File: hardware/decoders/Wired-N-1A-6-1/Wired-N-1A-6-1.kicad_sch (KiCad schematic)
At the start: 53 parts, among them J0 CA, J1 CA, J10 RL, J11 RR, J12 FOF, J13 F0R, J14 MCLR, J15 +5, J16 GND, J17 PGD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

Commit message: Made Wired-N-1A-6-1 prettier, and easier to follow.
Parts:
- C11, C12: value 1uF -> 2.2uF; MPN1 (none) -> GRM155R6YA225KE11D; Specification 0805 50V 10uF X5R 10% -> 0402 35V 2.2uF X5R 10%
- C21, C23: MPN1 (none) -> GRM033R61E104KE14D; Specification 0402 50V 100nF X7R 10% -> 0201 25V 100nF X5R 10%
- C31: footprint Capacitor_SMD:C_0201_0603Metric -> Capacitor_SMD:C_0402_1005Metric; MPN1 (none) -> GRM155R61H104KE14D; Specification 0402 50V 100nF X7R 10% -> 0402 50V 100nF X5R 10%
- D11, D12, D13, D14: MPN1 (none) -> MSK4010
- J0, J1, J10, J11, J12, J13, J14, J15, J16, J17, J18, J2, J3, J4, J5, J6, J7, J8, J9: MPN1 (none) -> DNP; MPN2 (none) -> DNP
- Q31, Q32: MPN1 (none) -> QH8MA3 QH8MA3
- Q41, Q42, Q43, Q44: MPN1 (none) -> 2N7002KD
- R21, R36: MPN1 (none) -> 0201WMF1331TEE; MPN2 (none) -> RC0201FR-071K33L; Specification 0402 1.33K Ω 1% 1/8W -> 0201 1.33K Ω 1% 1/8W
- R22, R35: MPN1 (none) -> 0201WMF665KTEE; MPN2 (none) -> RC0603F6R65CS; Specification 0402 6.65K Ω 1% 1/8W -> 0201 6.65K Ω 1% 1/8W
- R23: MPN1 (none) -> 0201WMF1002TEE; MPN2 (none) -> RC0201FR-0710KL; Specification 0402 10K Ω 1% 1/8W -> 0201 10K Ω 1% 1/8W
- R31, R32, R33, R34, R41, R42, R43, R44, R45, R46, R47, R48: MPN1 (none) -> 0201WMF2200TEE; MPN2 (none) -> RC0201FR-07220RL; Specification 0402 220 Ω 1% 1/8W -> 0201 220 Ω 1% 1/8W
- U11: value LR8341A-T50 -> LR8341A; MPN1 (none) -> LR8341A-T50
- U21: value PIC18F06Q40 -> PIC18F; MPN1 (none) -> PIC18F06Q40
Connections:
- net BackEMF: now also U21.4 (PGM/C12IN3-/RC3); no longer U21.6 (RC7)
- net F0R: now also U21.6 (RC7); no longer U21.5 (T1CKI/SS1/RC6)
- net F6: now also U21.5 (T1CKI/SS1/RC6); no longer U21.4 (PGM/C12IN3-/RC3)

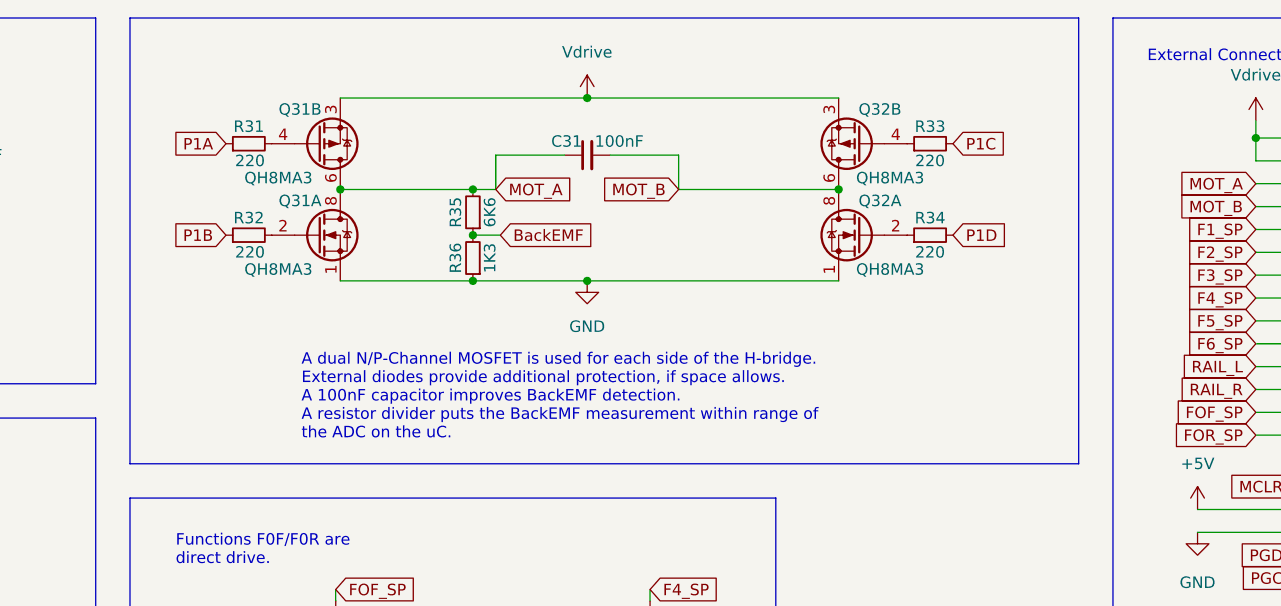
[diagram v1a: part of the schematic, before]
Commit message: Bring inline with Breadboard-1 reference design.
Add digital transitor drivers for the high side of the H-Bridge.
Add third BEMF resistor.
Relocate noise capacitor.
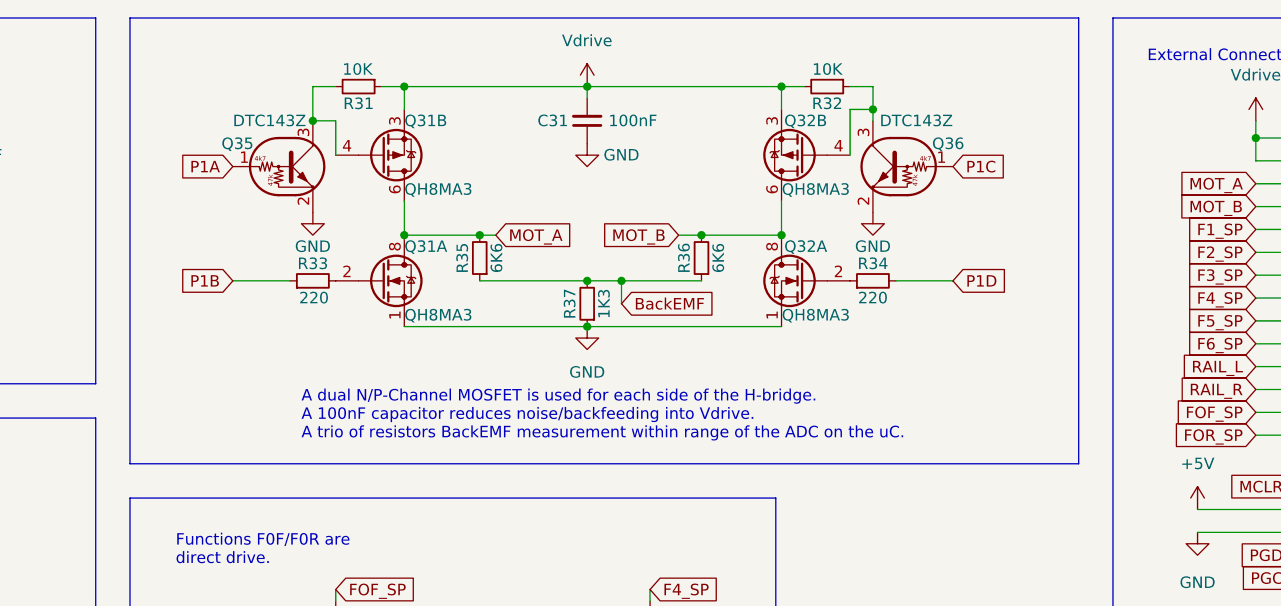
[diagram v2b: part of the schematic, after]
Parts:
- added Q35, Q36: DTC143Z, Package_TO_SOT_SMD:SOT-723, symbol Transistor_BJT:DTC143Z
- added R36: 6K6, Resistor_SMD:R_0201_0603Metric, symbol Device:R_Small
- R31: value 220 -> 10K
- R32: renamed from R33; value 220 -> 10K
- renumbered R32 to R33, R36 to R37
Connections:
- net BackEMF: now also R36.1
- net GND: now also C31.1, Q35.2 (E), Q36.2 (E)
- net MOT_A: no longer C31.1
- net MOT_B: now also R36.2; no longer C31.2
- net P1A: now also Q35.1 (B); no longer R31.1
- net P1C: now also Q36.1 (B); no longer R32.2
- net Vdrive: now also C31.2, R31.1, R32.2
- net at Q32.4 (G), R32.1: now also Q36.3 (C)
- net at Q31.4 (G), R31.2: now also Q35.3 (C)
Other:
- note added: "A dual N/P-Channel MOSFET is used for each side of the H-bridge. A 100nF capacitor reduces noise/backfeeding into Vdrive. A trio of resistors BackEMF measurement within range of the ADC on the uC."
- note removed: "A dual N/P-Channel MOSFET is used for each side of the H-bridge. External diodes provide additional protection, if space allows. A 100nF capacitor improves BackEMF detection. A resistor divider puts the BackEMF measurement within range of the ADC on the uC."
- moved on the sheet: C31, Q31A, Q31B, Q32A, Q32B, R31, R32, R33, R34, R35, R37
